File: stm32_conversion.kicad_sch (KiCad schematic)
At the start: 42 parts, among them IC2 LM3940IMP-3.3_NOPB, J1 Conn_01x04, J2 Micro_SD_Card, P1 USB_C_Plug_USB2.0, U2 TXB0108PW, U3 TXB0108PW, U4 W25Q16JVSS, Y1 Crystal_GND23

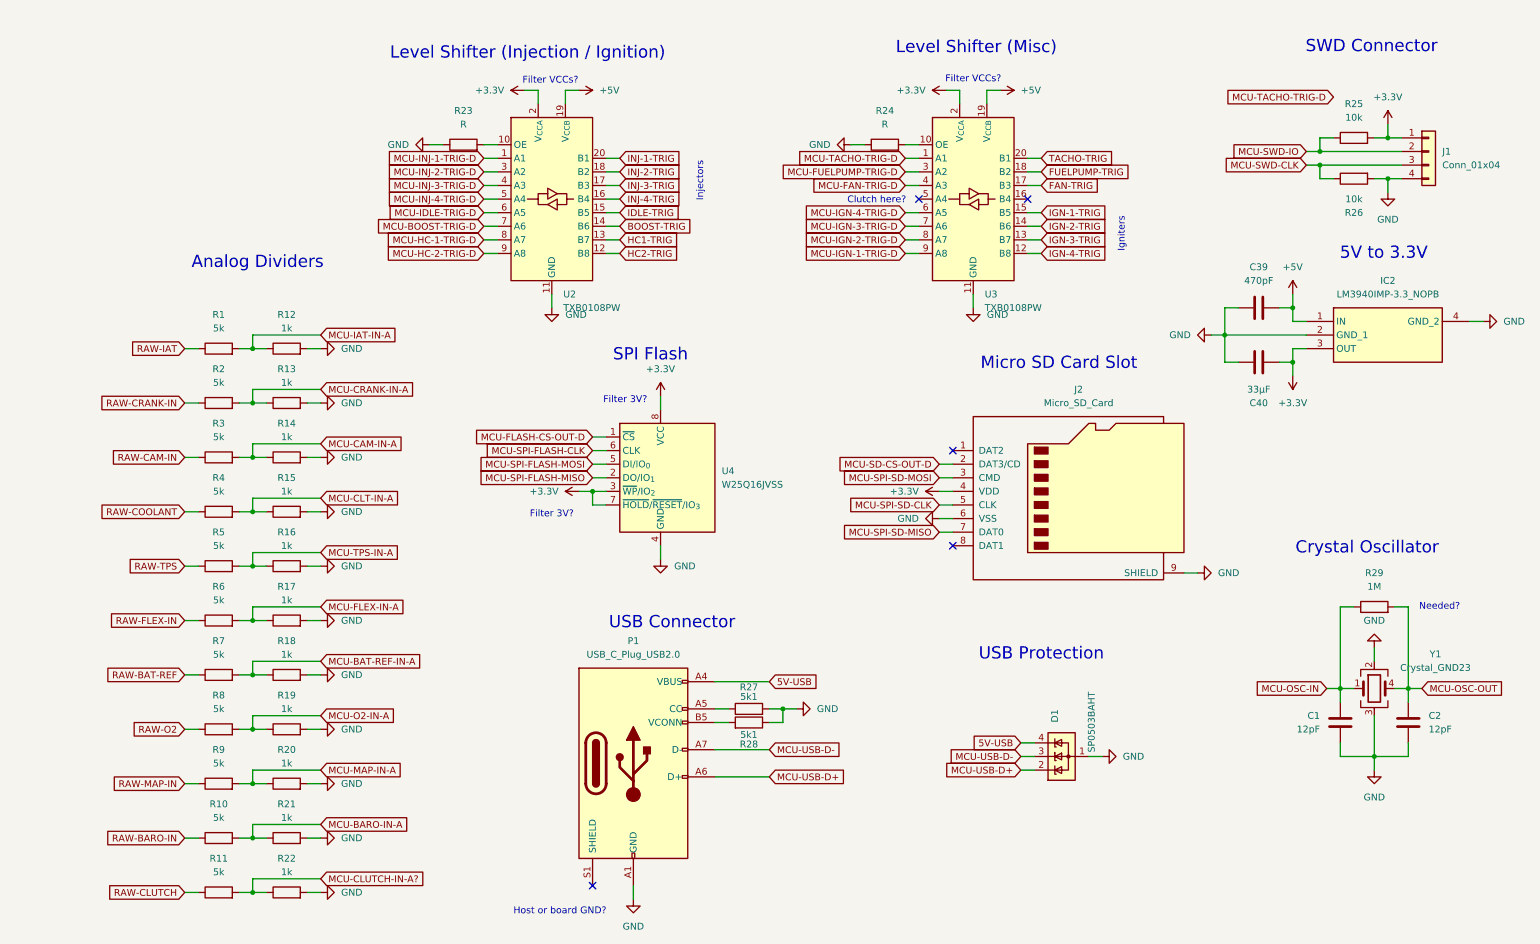
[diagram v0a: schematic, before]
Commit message: Add additional IOs
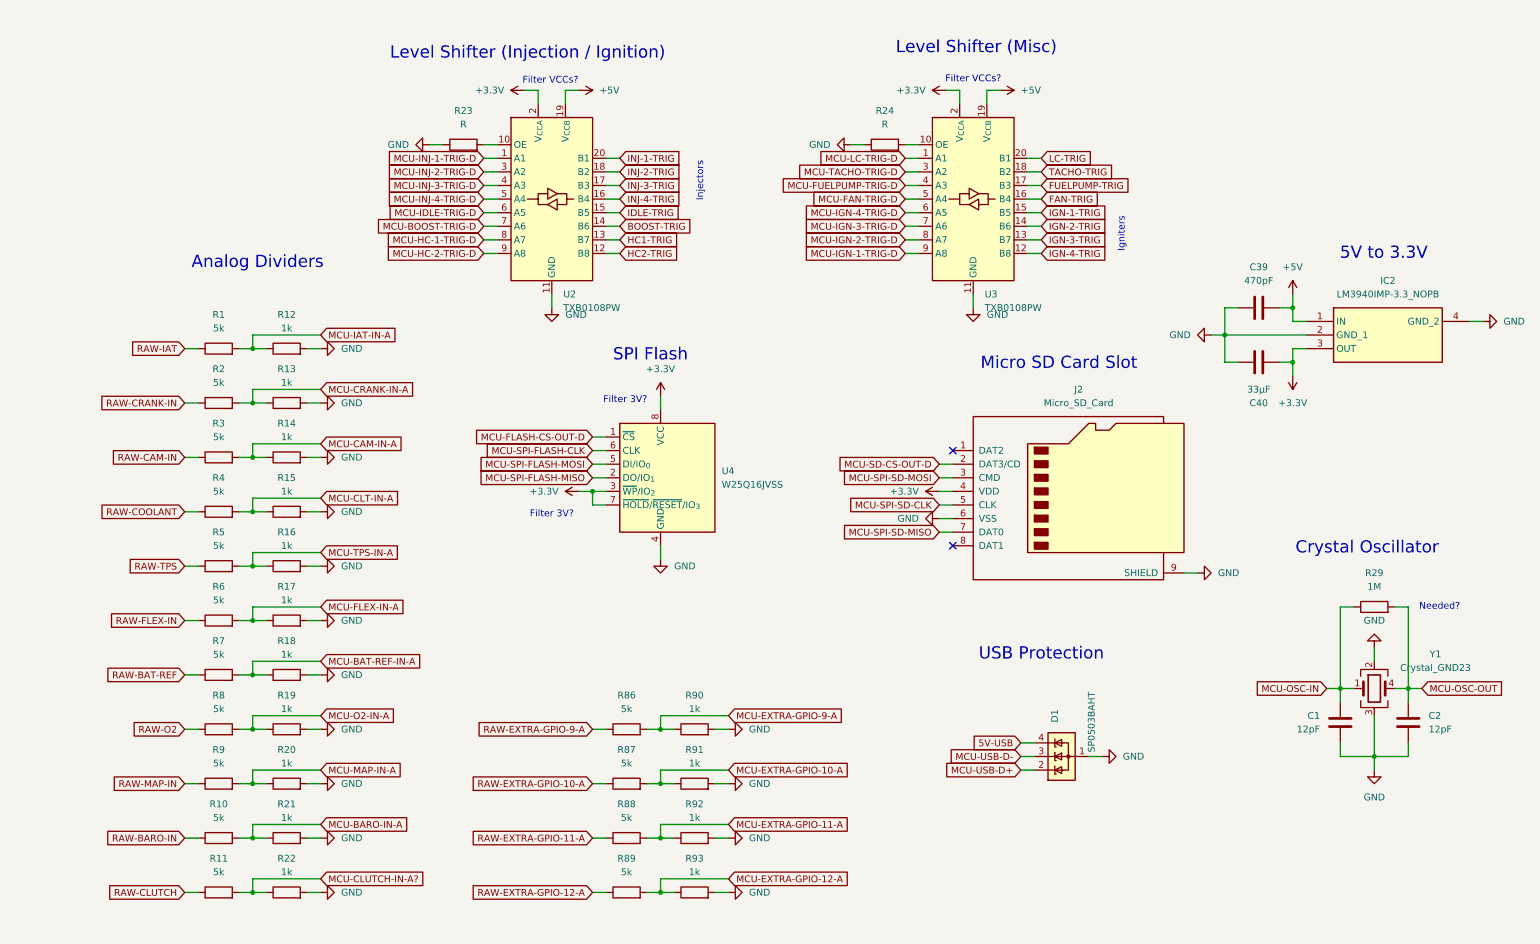
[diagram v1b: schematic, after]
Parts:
- removed J1: Conn_01x04, Connector_PinHeader_2.54mm:PinHeader_1x04_P2.54mm_Vertical, symbol Connector_Generic:Conn_01x04
- removed P1: USB_C_Plug_USB2.0, Connector_USB:USB_C_Receptacle_Palconn_UTC16-G, symbol Connector:USB_C_Plug_USB2.0
- removed R25, R26: 10k, Resistor_SMD:R_0805_2012Metric, symbol Device:R
- removed R27, R28: 5k1, Resistor_SMD:R_0805_2012Metric, symbol Device:R
- added R86, R87, R88, R89: 5k, Resistor_SMD:R_0805_2012Metric, symbol Device:R
- added R90, R91, R92, R93: 1k, Resistor_SMD:R_0805_2012Metric, symbol Device:R
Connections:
- net FAN-TRIG: now also U3.16 (B4); no longer U3.17 (B3)
- net FUELPUMP-TRIG: now also U3.17 (B3); no longer U3.18 (B2)
- net GND: now also R90.2, R91.2, R92.2, R93.2
- net MCU-FAN-TRIG-D: now also U3.5 (A4); no longer U3.4 (A3)
- net MCU-FUELPUMP-TRIG-D: now also U3.4 (A3); no longer U3.3 (A2)
- net MCU-TACHO-TRIG-D: now also U3.3 (A2); no longer U3.1 (A1)
- net TACHO-TRIG: now also U3.18 (B2); no longer U3.20 (B1)
- new net LC-TRIG: U3.20 (B1)
- new net MCU-EXTRA-GPIO-10-A: R87.2, R91.1
- new net MCU-EXTRA-GPIO-11-A: R88.2, R92.1
- new net MCU-EXTRA-GPIO-12-A: R89.2, R93.1
- new net MCU-EXTRA-GPIO-9-A: R86.2, R90.1
- new net MCU-LC-TRIG-D: U3.1 (A1)
- new net RAW-EXTRA-GPIO-10-A: R87.1
- new net RAW-EXTRA-GPIO-11-A: R88.1
- new net RAW-EXTRA-GPIO-12-A: R89.1
- new net RAW-EXTRA-GPIO-9-A: R86.1
- no-connect marks 5 -> 2
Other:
- note removed: "Clutch here?"
- note removed: "Host or board GND?"
- note removed: "SWD Connector"
- note removed: "USB Connector"

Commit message: Pre MCU switch
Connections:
- net MCU-IGN-1-TRIG-D: now also U3.6 (A5); no longer U3.9 (A8)
- net MCU-IGN-2-TRIG-D: now also U3.7 (A6); no longer U3.8 (A7)
- net MCU-IGN-3-TRIG-D: now also U3.8 (A7); no longer U3.7 (A6)
- net MCU-IGN-4-TRIG-D: now also U3.9 (A8); no longer U3.6 (A5)
- net RAW-BAT-REF renamed RAW-BAT

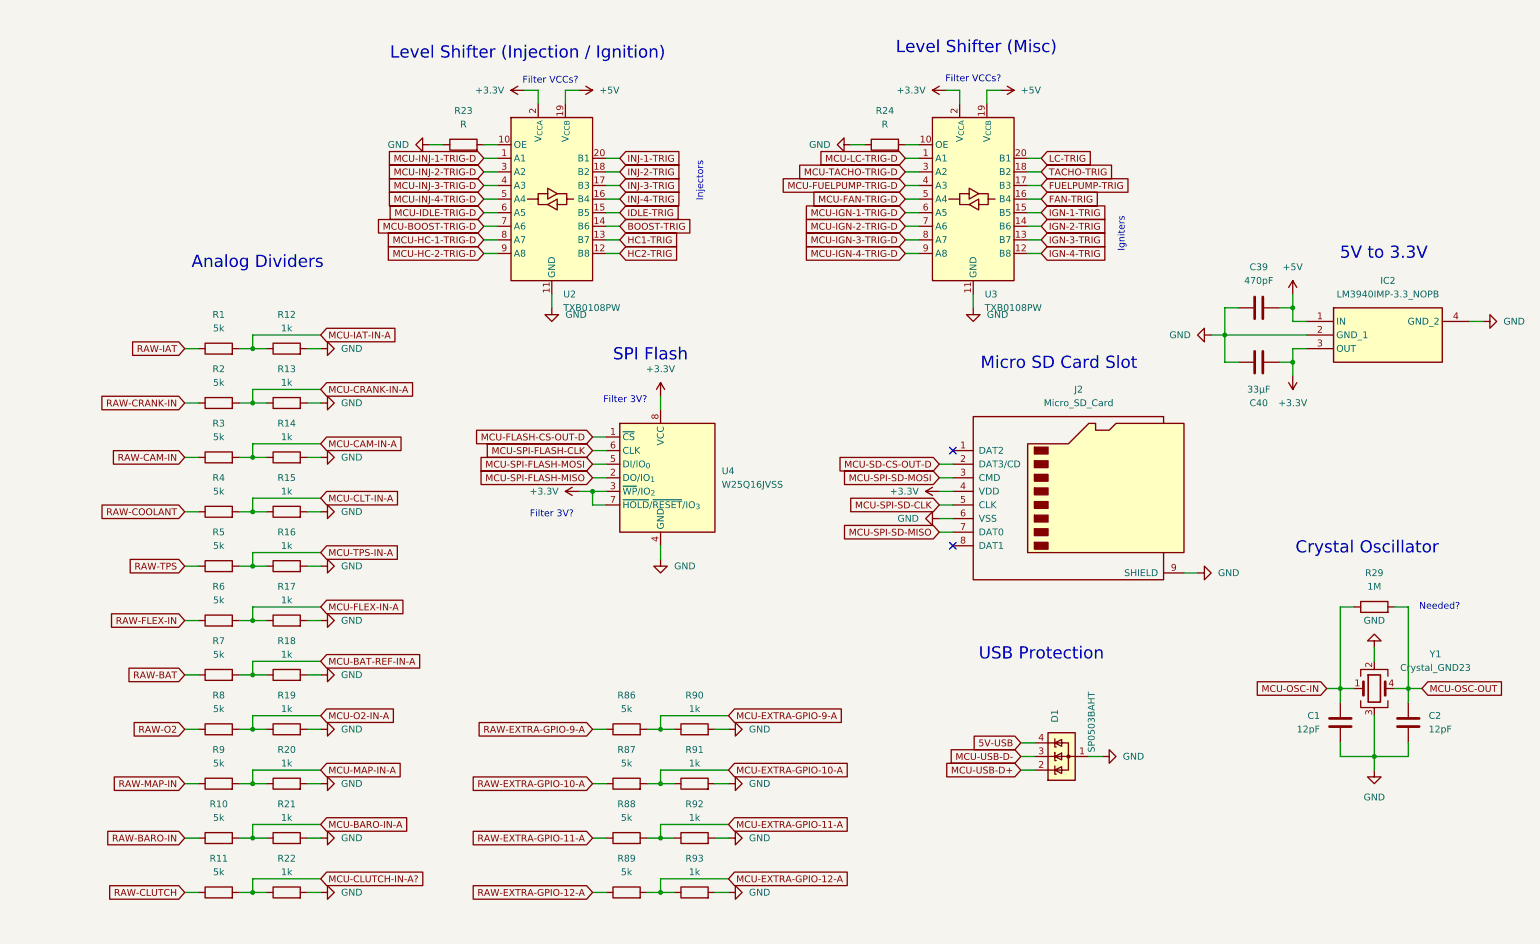
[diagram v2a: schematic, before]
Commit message: Update from Speeduino Discord suggestions (thanks to Detonator)
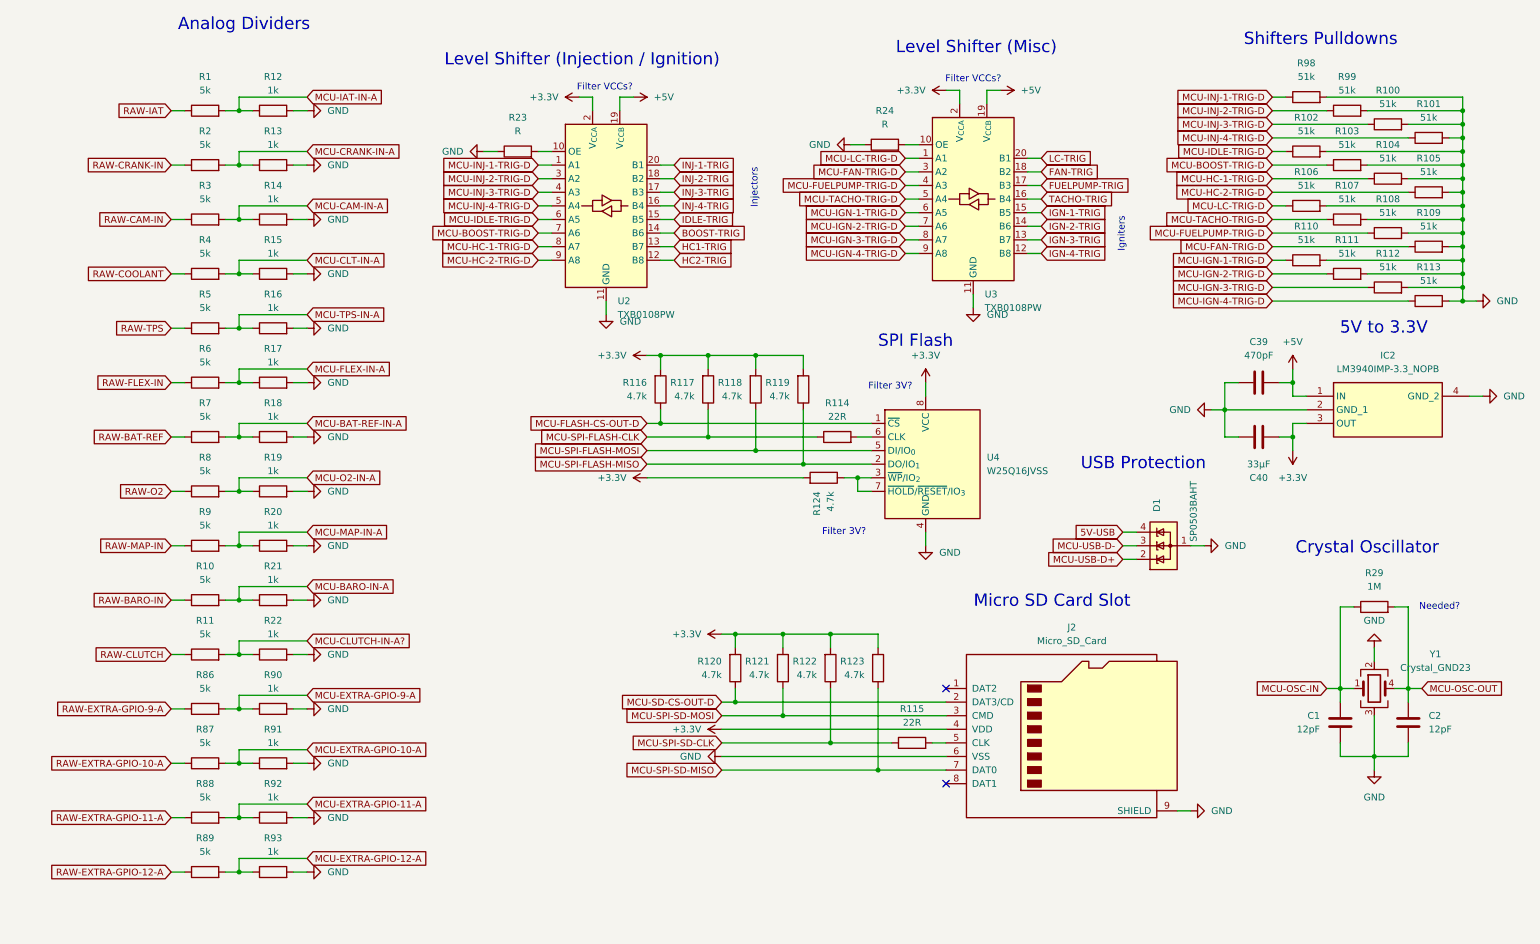
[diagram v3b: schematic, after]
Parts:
- added R100, R101, R102, R103, R104, R105, R106, R107, R108, R109, R110, R111, R112, R113, R98, R99: 51k, Resistor_SMD:R_0805_2012Metric, symbol Device:R
- added R114, R115: 22R, Resistor_SMD:R_0805_2012Metric, symbol Device:R
- added R116, R117, R118, R119, R120, R121, R122, R123, R124: 4.7k, Resistor_SMD:R_0805_2012Metric, symbol Device:R
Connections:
- net +3.3V: now also R116.2, R117.2, R118.2, R119.2, R120.2, R121.2, R122.2, R123.2, R124.2; no longer U4.3 (~{WP}/IO_{2}), U4.7 (~{HOLD}/~{RESET}/IO_{3})
- net FAN-TRIG: now also U3.18 (B2); no longer U3.16 (B4)
- net GND: now also R100.2, R101.2, R102.2, R103.2, R104.2, R105.2, R106.2, R107.2, R108.2, R109.2, R110.2, R111.2, R112.2, R113.2, R98.2, R99.2
- net MCU-BOOST-TRIG-D: now also R103.1
- net MCU-FAN-TRIG-D: now also U3.3 (A2), R109.1; no longer U3.5 (A4)
- net MCU-FLASH-CS-OUT-D: now also R116.1
- net MCU-FUELPUMP-TRIG-D: now also R108.1
- net MCU-HC-1-TRIG-D: now also R104.1
- net MCU-HC-2-TRIG-D: now also R105.1
- net MCU-IDLE-TRIG-D: now also R102.1
- net MCU-IGN-1-TRIG-D: now also R110.1
- net MCU-IGN-2-TRIG-D: now also R111.1
- net MCU-IGN-3-TRIG-D: now also R112.1
- net MCU-IGN-4-TRIG-D: now also R113.1
- net MCU-INJ-1-TRIG-D: now also R98.1
- net MCU-INJ-2-TRIG-D: now also R99.1
- net MCU-INJ-3-TRIG-D: now also R100.1
- net MCU-INJ-4-TRIG-D: now also R101.1
- net MCU-LC-TRIG-D: now also R106.1
- net MCU-SD-CS-OUT-D: now also R120.1
- net MCU-SPI-FLASH-CLK: now also R114.1, R117.1; no longer U4.6 (CLK)
- net MCU-SPI-FLASH-MISO: now also R119.1
- net MCU-SPI-FLASH-MOSI: now also R118.1
- net MCU-SPI-SD-CLK: now also R115.1, R122.1; no longer J2.5 (CLK)
- net MCU-SPI-SD-MISO: now also R123.1
- net MCU-SPI-SD-MOSI: now also R121.1
- net MCU-TACHO-TRIG-D: now also U3.5 (A4), R107.1; no longer U3.3 (A2)
- net TACHO-TRIG: now also U3.16 (B4); no longer U3.18 (B2)
- net RAW-BAT renamed RAW-BAT-REF
- new net: R124.1, U4.3 (~{WP}/IO_{2}), U4.7 (~{HOLD}/~{RESET}/IO_{3})
- new net: R114.2, U4.6 (CLK)
- new net: J2.5 (CLK), R115.2
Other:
- note added: "Shifters Pulldowns"
- moved on the sheet: C39, C40, D1, IC2, J2, R1, R10, R11, R12, R13, R14, R15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
